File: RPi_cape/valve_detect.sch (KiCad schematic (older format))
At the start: 22 parts, among them Q1 MMBT3904, U36 LMC7101B, U37 LMC7101B

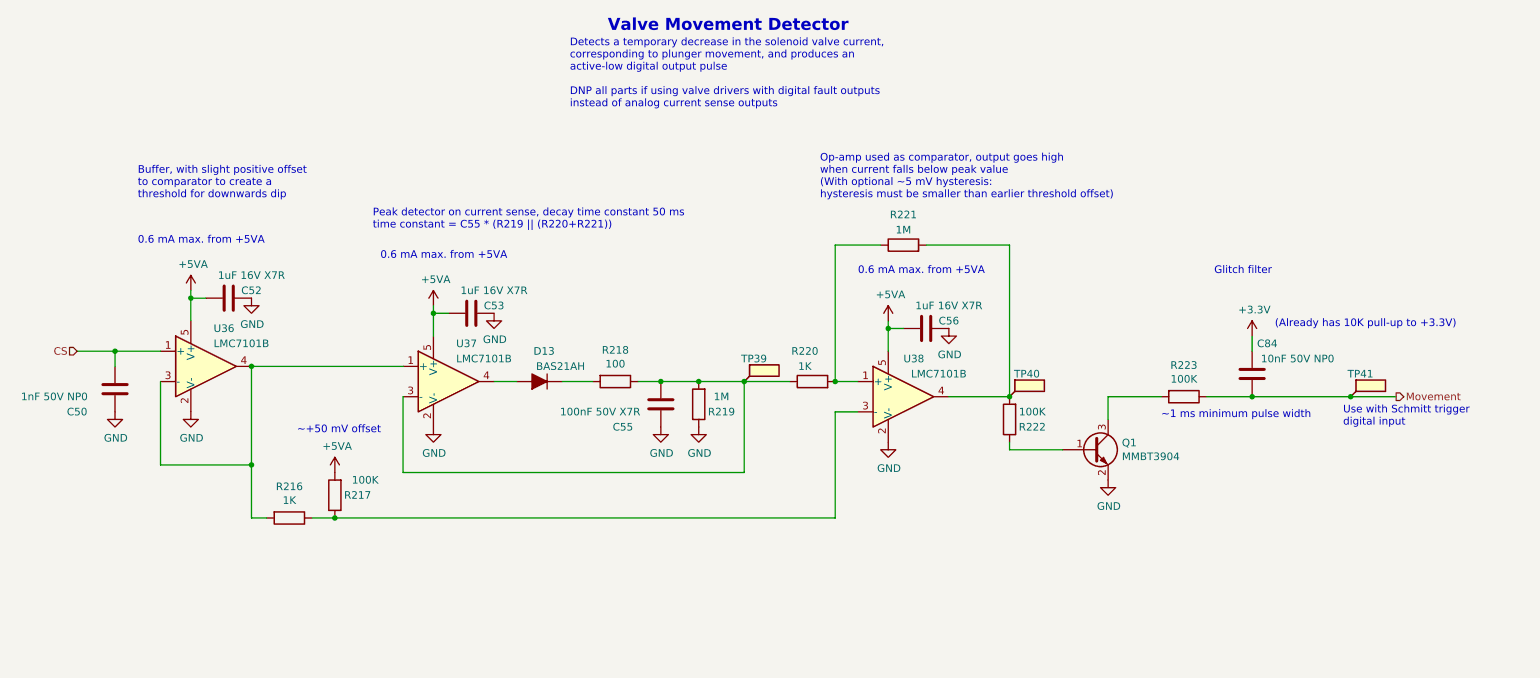
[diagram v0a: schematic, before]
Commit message: Analog upgrades and extra encoder connectors
Renamed a few files
Removed "costing BOM" as difficult to keep up to date, easy to regenerate
Toughened under-voltage detect circuits by adding hysteresis to +5V detect for +BATT diode-OR (R236), filtering to power-down alarm detect input (C85)
Added connector options (J15, J21) for Grayhill C14-series rotary encoder with cable
Changed R190 from 3K to 2.4K to increase overhead on base current required for saturation, and consolidate BOM
Added 3 solderable testpoints for expanding CPLD pin options (TP44-46), adjusted some CPLD pin assignments to allow physical routing to pins
Fixed valve motion detector by changing comparator's hysteresis to AC-only, changing NPN's series resistor to 1K (allows low-enough DC level to count as logic low), and adding optional filtering cap C115 to offset divider
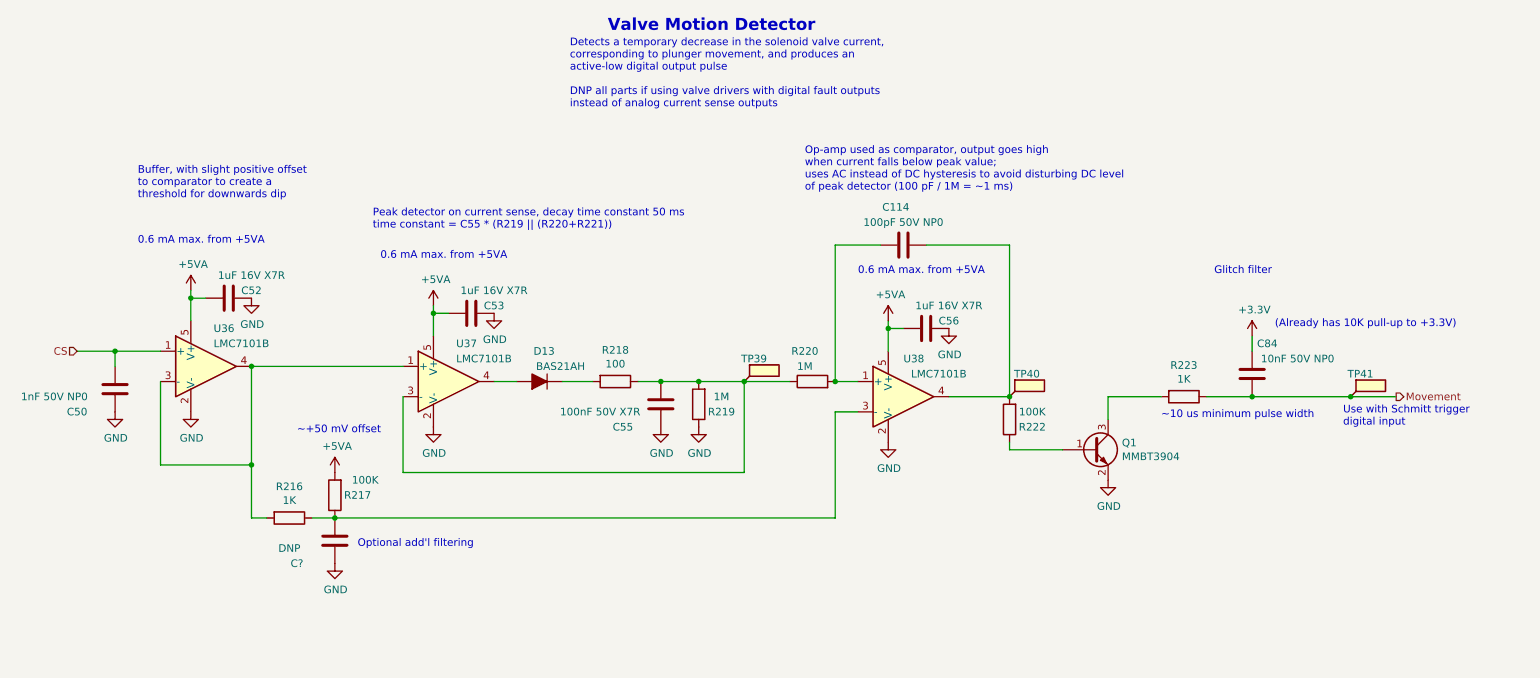
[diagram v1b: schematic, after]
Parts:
- removed R221: 1M, Resistor_SMD:R_1206_3216Metric, symbol Device:R
- added C114: 100pF 50V NP0, Capacitor_SMD:C_0603_1608Metric, symbol Device:C
- added C?: DNP, Capacitor_SMD:C_0603_1608Metric, symbol Device:C
- R219: value 100K -> 1K; Part Number RK73H2BTTD1003F -> RK73H2BTTD1001F
- R220: value 1K -> 1M; Part Number RK73H2BTTD1001F -> RK73H2BTTD1004F
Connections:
- net GND: now also C?.1
- net at R220.2, U37.1 (+): now also C114.1
- net at R216.1, R217.1, U37.3 (-): now also C?.2
- net at R218.2, TP40.1, U37.4: now also C114.2
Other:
- note added: "Op-amp used as comparator, output goes high\nwhen current falls below peak value;\nuses AC instead of DC hysteresis to avoid disturbing DC level\nof peak detector (100 pF / 1M = ~~1 ms)"
- note added: "Optional add'l filtering"
- note added: "Valve Motion Detector"
- note added: "~~10 us minimum pulse width"
- note removed: "Op-amp used as comparator, output goes high\nwhen current falls below peak value\n(With optional ~~5 mV hysteresis:\nhysteresis must be smaller than earlier threshold offset)"
- note removed: "Valve Movement Detector"
- note removed: "~~1 ms minimum pulse width"
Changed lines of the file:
@@
 encoding utf-8
 Sheet 14 15
-Title "Valve Movement Detection"
+Title "Raspberry Pi Hat for JamVent Adaptation"
 Date ""
-Rev "1.7"
+Rev "1.8"
 Comp "US JamVent Team"
 Comment1 "Don Straney"
@@
 AR Path="/60304D29/60224EAB" Ref="R223"  Part="1"
 F 0 "R223" V 8993 3400 50  0000 C CNN
-F 1 "100K" V 9084 3400 50  0000 C CNN
+F 1 "1K" V 9084 3400 50  0000 C CNN
 F 2 "Resistor_SMD:R_1206_3216Metric" V 9130 3400 50  0001 C CNN
 F 3 "~" H 9200 3400 50  0001 C CNN
 F 4 "KOA Speer" H 9200 3400 50  0001 C CNN "Manufacturer"
-F 5 "RK73H2BTTD1003F" H 9200 3400 50  0001 C CNN "Part Number"
+F 5 "RK73H2BTTD1001F" H 9200 3400 50  0001 C CNN "Part Number"
 	1    9200 3400
 	0    1    1    0
@@
 	8050 3750 8400 3750
 Text Notes 9050 3550 0    50   ~ 0
-~~1 ms minimum pulse width
+~~10 us minimum pulse width
 $Comp
 L Connector:TestPoint_Flag TP?
@@
 Text Notes 3850 2300 0    50   ~ 0
 Peak detector on current sense, decay time constant 50 ms\ntime constant = C55 * (R219 || (R220+R221))
-Text Notes 6800 2100 0    50   ~ 0
-Op-amp used as comparator, output goes high\nwhen current falls below peak value\n(With optional ~~5 mV hysteresis:\nhysteresis must be smaller than earlier threshold offset)
+Text Notes 6700 2050 0    50   ~ 0
+Op-amp used as comparator, output goes high\nwhen current falls below peak value;\nuses AC instead of DC hysteresis to avoid disturbing DC level\nof peak detector (100 pF / 1M = ~~1 ms)
 Text Notes 9400 2600 0    50   ~ 0
 Glitch filter
@@
 AR Path="/60304D29/60277704" Ref="R220"  Part="1"
 F 0 "R220" V 6950 3350 50  0000 C CNN
-F 1 "1K" V 6850 3350 50  0000 C CNN
+F 1 "1M" V 6850 3350 50  0000 C CNN
 F 2 "Resistor_SMD:R_1206_3216Metric" V 6680 3300 50  0001 C CNN
 F 3 "~" H 6750 3300 50  0001 C CNN
 F 4 "KOA Speer" H 6750 3300 50  0001 C CNN "Manufacturer"
-F 5 "RK73H2BTTD1001F" H 6750 3300 50  0001 C CNN "Part Number"
+F 5 "RK73H2BTTD1004F" H 6750 3300 50  0001 C CNN "Part Number"
 	1    6750 3300
 	0    -1   -1   0
@@
 Wire Wire Line
 	6900 3300 7050 3300
-$Comp
-L Device:R R?
-U 1 1 60279BA3
-P 7350 2400
-AR Path="/60279BA3" Ref="R?"  Part="1"
-AR Path="/5E8AFE9D/60279BA3" Ref="R?"  Part="1"
-AR Path="/5E8A4ABF/60279BA3" Ref="R?"  Part="1"
-AR Path="/601431F1/60279BA3" Ref="R?"  Part="1"
-AR Path="/60304D29/60279BA3" Ref="R221"  Part="1"
-F 0 "R221" V 7550 2400 50  0000 C CNN
-F 1 "1M" V 7450 2400 50  0000 C CNN
-F 2 "Resistor_SMD:R_1206_3216Metric" V 7280 2400 50  0001 C CNN
-F 3 "~" H 7350 2400 50  0001 C CNN
-F 4 "KOA Speer" H 7350 2400 50  0001 C CNN "Manufacturer"
-F 5 "RK73H2BTTD1004F" H 7350 2400 50  0001 C CNN "Part Number"
-	1    7350 2400
-	0    -1   -1   0
-$EndComp
 Wire Wire Line
 	7200 2400 6900 2400
@@
 	3600 4200 6900 4200
 Text Notes 5400 1000 0    79   ~ 16
-Valve Movement Detector
+Valve Motion Detector
 $Comp
 L power:GND #PWR?
@@
 Text Notes 9800 2950 0    50   ~ 0
 (Already has 10K pull-up to +3.3V)
+$Comp
+L Device:C C?
+U 1 1 5F28A2C9
+P 7350 2400
+AR Path="/5F28A2C9" Ref="C?"  Part="1"
+AR Path="/5E8AFE9D/5F28A2C9" Ref="C?"  Part="1"
+AR Path="/5E8A4ABF/5F28A2C9" Ref="C?"  Part="1"
+AR Path="/601431F1/5F28A2C9" Ref="C?"  Part="1"
+AR Path="/60304D29/5F28A2C9" Ref="C114"  Part="1"
+F 0 "C114" V 7600 2450 50  0000 C CNN
+F 1 "100pF 50V NP0" V 7500 2400 50  0000 C CNN
+F 2 "Capacitor_SMD:C_0603_1608Metric" H 7388 2250 50  0001 C CNN
+F 3 "~" H 7350 2400 50  0001 C CNN
+F 4 "Kemet" H 7350 2400 50  0001 C CNN "Manufacturer"
+F 5 "C0603C101J5GACTU" H 7350 2400 50  0001 C CNN "Part Number"
+	1    7350 2400
+	0    -1   -1   0
+$EndComp
+$Comp
+L Device:C C?
+U 1 1 5F299EA1
+P 3600 4350
+AR Path="/5F299EA1" Ref="C?"  Part="1"
+AR Path="/5E8AFE9D/5F299EA1" Ref="C?"  Part="1"
+AR Path="/5E8A4ABF/5F299EA1" Ref="C?"  Part="1"
+AR Path="/601431F1/5F299EA1" Ref="C?"  Part="1"
+AR Path="/60304D29/5F299EA1" Ref="C?"  Part="1"
+F 0 "C?" H 3850 4500 50  0000 C CNN
+F 1 "DNP" H 3900 4400 50  0000 C CNN
+F 2 "Capacitor_SMD:C_0603_1608Metric" H 3638 4200 50  0001 C CNN
+F 3 "~" H 3600 4350 50  0001 C CNN
+F 4 "" H 3600 4350 50  0001 C CNN "Manufacturer"
+F 5 "" H 3600 4350 50  0001 C CNN "Part Number"
+	1    3600 4350
+	-1   0    0    1
+$EndComp
+$Comp
+L power:GND #PWR?
+U 1 1 5F299EA7
+P 3600 4500
+AR Path="/5F299EA7" Ref="#PWR?"  Part="1"
+AR Path="/5E8AFE9D/5F299EA7" Ref="#PWR?"  Part="1"
+AR Path="/5E8A4ABF/5F299EA7" Ref="#PWR?"  Part="1"
+AR Path="/601431F1/5F299EA7" Ref="#PWR?"  Part="1"
+AR Path="/60304D29/5F299EA7" Ref="#PWR?"  Part="1"
+F 0 "#PWR?" H 3600 4250 50  0001 C CNN
+F 1 "GND" H 3605 4327 50  0000 C CNN
+F 2 "" H 3600 4500 50  0001 C CNN
+F 3 "" H 3600 4500 50  0001 C CNN
+	1    3600 4500
+	1    0    0    -1
+$EndComp
+Text Notes 3750 4400 0    50   ~ 0
+Optional add'l filtering
 $EndSCHEMATC

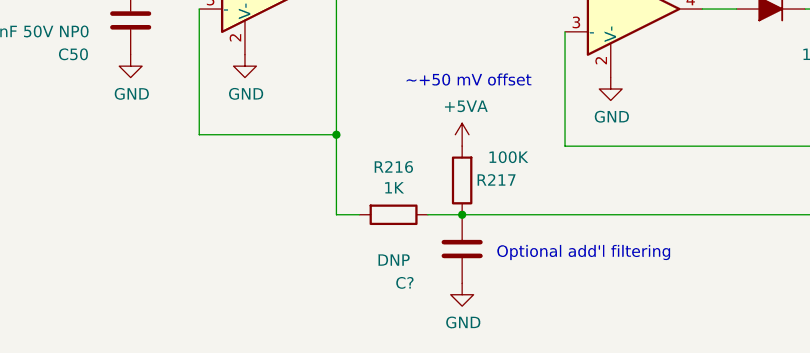
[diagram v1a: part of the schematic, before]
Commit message: Updates based on testing, extra documentation
Added thermal calculations, possible thermal-induced problems to fault-condition list
Renamed error calculations file
Added some bringup tests
Changed 24V LED resistors (R20, R22) to 24.9K to consolidate BOM
Adjusted audio amp volume and filtering according to breadboard experiments
Moved bottom-end mounting holes and encoder connectors to avoid interfering mechanically with Raspberry Pi
Replaced under-sized power-ORing diodes with better Schottky option, added heatsinking with copper planes
Improved LMZ14203 heatsinking by removing thermal reliefs, re-arranging input-current-measurement testpoints to increase top-layer copper area
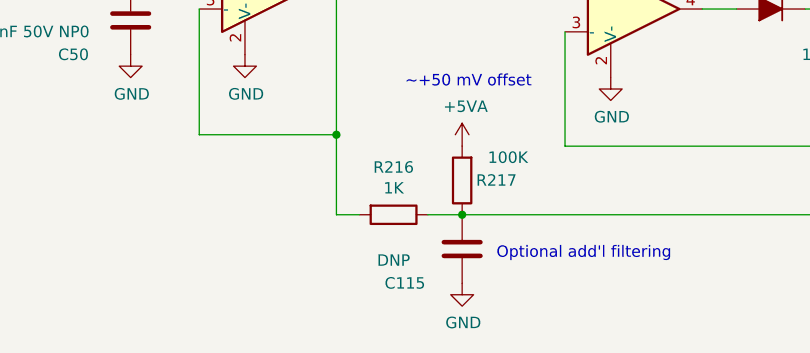
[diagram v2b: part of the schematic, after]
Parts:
- gave numbers to parts that had none: 1
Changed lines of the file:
@@
 Title "Raspberry Pi Hat for JamVent Adaptation"
 Date ""
-Rev "1.8"
+Rev "1.9"
 Comp "US JamVent Team"
 Comment1 "Don Straney"
@@
 AR Path="/5E8A4ABF/5F299EA1" Ref="C?"  Part="1"
 AR Path="/601431F1/5F299EA1" Ref="C?"  Part="1"
-AR Path="/60304D29/5F299EA1" Ref="C?"  Part="1"
-F 0 "C?" H 3850 4500 50  0000 C CNN
+AR Path="/60304D29/5F299EA1" Ref="C115"  Part="1"
+F 0 "C115" H 3850 4500 50  0000 C CNN
 F 1 "DNP" H 3900 4400 50  0000 C CNN
 F 2 "Capacitor_SMD:C_0603_1608Metric" H 3638 4200 50  0001 C CNN
@@
 AR Path="/5E8A4ABF/5F299EA7" Ref="#PWR?"  Part="1"
 AR Path="/601431F1/5F299EA7" Ref="#PWR?"  Part="1"
-AR Path="/60304D29/5F299EA7" Ref="#PWR?"  Part="1"
-F 0 "#PWR?" H 3600 4250 50  0001 C CNN
+AR Path="/60304D29/5F299EA7" Ref="#PWR0380"  Part="1"
+F 0 "#PWR0380" H 3600 4250 50  0001 C CNN
 F 1 "GND" H 3605 4327 50  0000 C CNN
 F 2 "" H 3600 4500 50  0001 C CNN

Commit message: Admin (naming, license), improvements based on testing
Updated name on schematic, PCB silkscreen
Added 3 mounting holes on inside area of board for better mechanical robustness
Removed extra unused pressure sensor barb packages from library
Fixed Phoenix spring connector footprints, and added 3D models from Phoenix website
Added 3D models to TE encoder connector footprints, QFP-100 for CPLD, and 5019 testpoint
Changed DIAG_EN pin connection from valve drivers from +24V (too high) to +3.3V
Added CERN licensing terms
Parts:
- TP39, TP40, TP41: footprint TestPoint:TestPoint_Keystone_5019_Minature -> Ventilator:TestPoint_Keystone_5019_Minature
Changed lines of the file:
@@
 encoding utf-8
 Sheet 14 15
-Title "Raspberry Pi Hat for JamVent Adaptation"
+Title "GlobalVent Stand-Alone Controller"
 Date ""
-Rev "1.9"
-Comp "US JamVent Team"
-Comment1 "Don Straney"
-Comment2 ""
+Rev "1.10"
+Comp "US GlobalVent Team"
+Comment1 "Licensed under CERN-OHL-S v2"
+Comment2 "Don Straney"
 Comment3 ""
 Comment4 ""
@@
 F 0 "TP39" H 6450 3450 50  0000 R CNN
 F 1 "TestPoint_Flag" H 6256 3303 50  0001 R CNN
-F 2 "TestPoint:TestPoint_Keystone_5019_Minature" H 6500 3300 50  0001 C CNN
+F 2 "Ventilator:TestPoint_Keystone_5019_Minature" H 6500 3300 50  0001 C CNN
 F 3 "~" H 6500 3300 50  0001 C CNN
 F 4 "Keystone" H 6300 3300 50  0001 C CNN "Manufacturer"
@@
 F 0 "TP40" H 8250 3550 50  0000 R CNN
 F 1 "TestPoint_Flag" H 8006 3403 50  0001 R CNN
-F 2 "TestPoint:TestPoint_Keystone_5019_Minature" H 8250 3400 50  0001 C CNN
+F 2 "Ventilator:TestPoint_Keystone_5019_Minature" H 8250 3400 50  0001 C CNN
 F 3 "~" H 8250 3400 50  0001 C CNN
 F 4 "Keystone" H 8050 3400 50  0001 C CNN "Manufacturer"
@@
 F 0 "TP41" H 10450 3550 50  0000 R CNN
 F 1 "TestPoint_Flag" H 10256 3403 50  0001 R CNN
-F 2 "TestPoint:TestPoint_Keystone_5019_Minature" H 10500 3400 50  0001 C CNN
+F 2 "Ventilator:TestPoint_Keystone_5019_Minature" H 10500 3400 50  0001 C CNN
 F 3 "~" H 10500 3400 50  0001 C CNN
 F 4 "Keystone" H 10300 3400 50  0001 C CNN "Manufacturer"

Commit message: Design update based on changed software/firmware/pneumatics reqs
Swapped Max V CPLD for Max 10 FPGA
Removed +1.8V regulator and monitoring (in power-down alarm) because Max 10 FPGA has internal regulator
Changed FPGA's valve-enable pull-downs from 1K to 10K because Max 10 floats the outputs during power-up/programming (instead of Max V's internal pull-ups)
Changed low-pressure sensor from BMP388 to MS5607 for more manufacturable footprint / high availability, and moved all digital pressure sensors to daughterboard for repairability
Changed single op-amps in analog pressure sensor inputs / valve motion detect circuits to TLV6001 for better bias current, correct footprint
Removed excessive DNP components in analog pressure sensor inputs to ease routing with new op-amps
Added double-inverted hysteresis circuit to valve motion detect that won't drive U38's '+' input above the rail and cause latchup
Added optional pull-down resistors to valve-motiion-detect op-amps to allow output voltages to swing to zero
Added optional filter caps to ADC sensor inputs
Added pull-down to O2 sensor input for testing with sensor unplugged
Increased ADC input resistors (in analog sensor inputs) from 1K to 3.3K to avoid "lifting" +3.3V rail voltage in case of fault
Increased hole sizes to 3.7 mm for fitting #6 screws, to match some threaded vibration-damping bumpers from Joost
Fixed F.Fab-layer component reference text in custom footprints
Updated manufacturing files
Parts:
- added C77: 100pF 50V NP0, Capacitor_SMD:C_0603_1608Metric, symbol Device:C
- added C81: DNP, Capacitor_SMD:C_0603_1608Metric, symbol Device:C
- added R202, R35, R36: DNP, Resistor_SMD:R_1206_3216Metric, symbol Device:R
- added R205: 0, Resistor_SMD:R_1206_3216Metric, symbol Device:R
- added R240: 100K, Resistor_SMD:R_1206_3216Metric, symbol Device:R
- C114: value 100pF 50V NP0 -> DNP; DNI (none) -> DNI; Manufacturer Kemet -> (none); Part Number C0603C101J5GACTU -> (none)
- C115: DNI (none) -> DNI
- C56: value 10nF 50V NP0 -> DNP; DNI (none) -> DNI; Manufacturer Murata -> (none); Part Number GRM1885C1H103JA01D -> (none)
- R219: value 1K -> 0; Manufacturer KOA Speer -> Panasonic; Part Number RK73H2BTTD1001F -> ERJ-8GEY0R00V
- R220: value 1M -> 0; Manufacturer KOA Speer -> Panasonic; Part Number RK73H2BTTD1004F -> ERJ-8GEY0R00V
- U36, U37: value LMC7101B -> TLV6001; symbol Amplifier_Operational:LMV321 -> Amplifier_Operational:MCP601-xOT; Part Number LMC7101BIM5/NOPB -> TLV6001IDBVR
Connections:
- net CS: now also U36.3 (+); no longer U36.1 (+)
- net GND: now also R35.2, R36.2
- net at C114.1, R220.2: now also U37.3 (+); no longer U37.1 (+)
- net at C114.2, R218.2, TP40.1: now also U37.1, C81.1; no longer U37.4
- net at C115.2, R216.1, R217.1: now also U37.4 (-), C77.1; no longer U37.3 (-)
- net at C53.2, R216.1, R217.2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: now also R205.1; no longer U36.3 (-)
- net at D13.1 (K), R216.2: now also R202.1
- net at R216.2, U36.4 (-): now also U36.1, U36.3 (+), R35.1; no longer U36.1 (+), U36.3 (-)
- net at U36.4 (-): now also R202.2, R205.2; no longer D13.2 (A)
- net at Q1.3 (C), R219.2: now also R240.2
- net at Q1.1 (B), R218.1: now also C81.2
- new net: C77.2, R240.1
- new net: D13.2 (A), R36.1, U36.1
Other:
- note added: "0.1 mA max. from +5VA"
- note added: "100K fbk from 3.3V collector voltage change,\ninto 1K source impedance on '-' input, creates\n~~33 mV hysteresis"
- note added: "Slow slew rate of 0.5 V/µs works\nas short de-glitch filter"
- note removed: "0.6 mA max. from +5VA"
- note removed: "Glitch filter"
- note removed: "~~10 us minimum pulse width"
- moved on the sheet: D13, TP40
